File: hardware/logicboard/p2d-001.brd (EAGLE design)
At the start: 91 x 90 mm, 55 parts, among them IC1 74LS06N, IC2 4066N, J1 MKR, J2 GPIO, J3 Vcc, J4 RLY, J5 SPI, J7 DIN5, J8 DIN5, J9 DIN5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

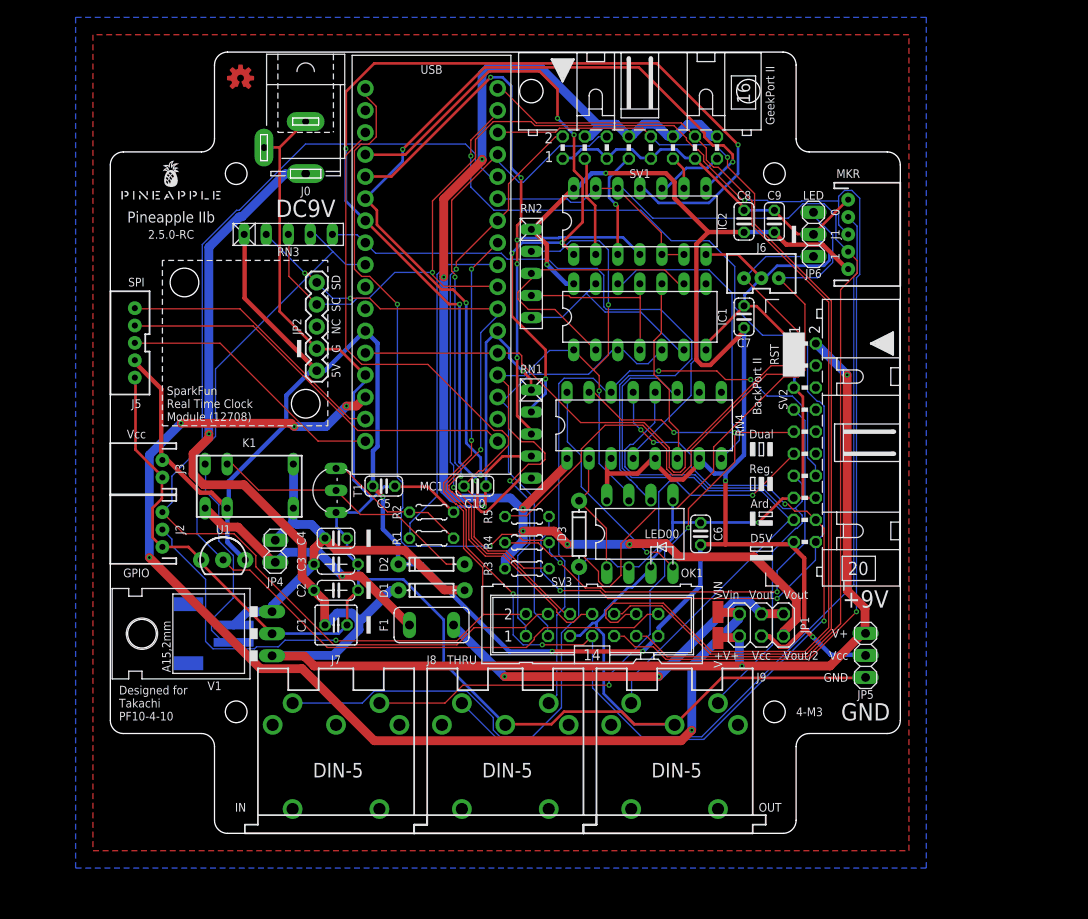
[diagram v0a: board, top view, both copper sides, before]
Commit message: Changed dimension of the board.
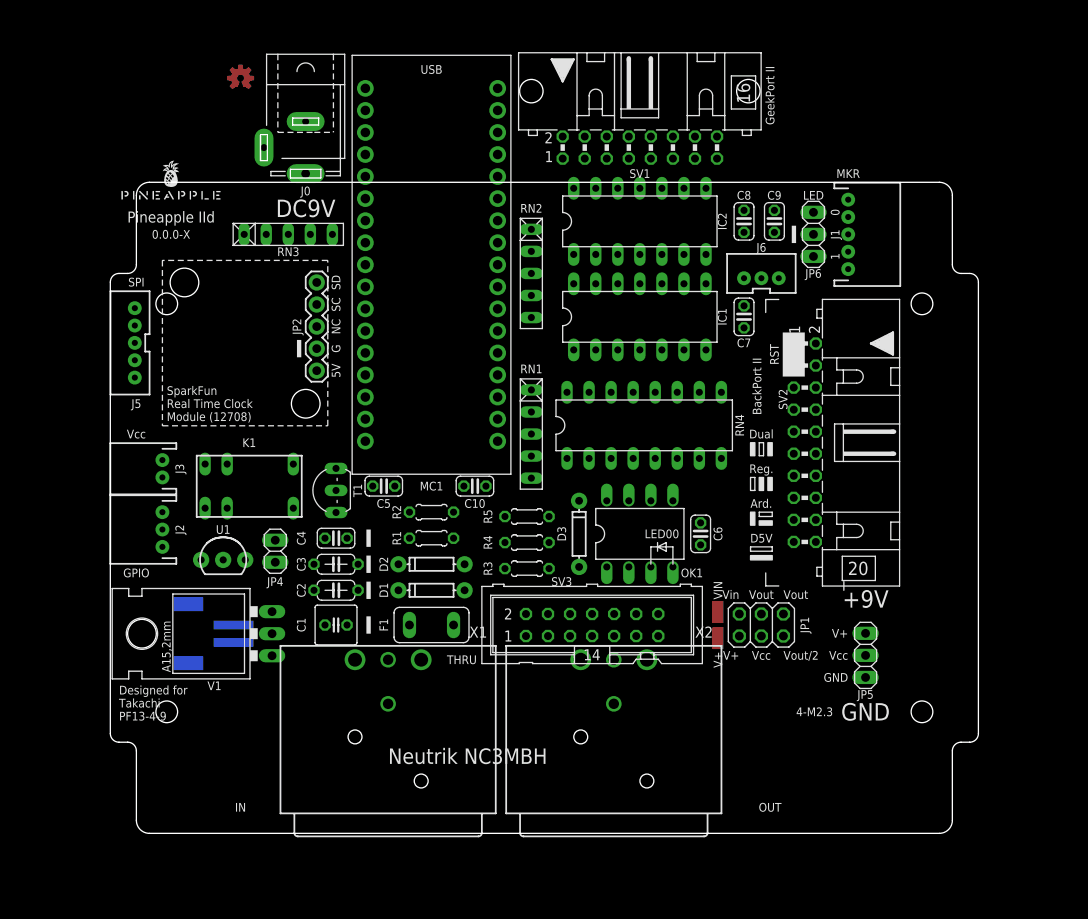
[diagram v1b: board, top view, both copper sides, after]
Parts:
- removed J7, J8, J9: DIN5, SparkFun-Connectors:DIN5-RA-PTH
- added X1, X2: NC3MBH, con-neutrik_ag:NC3MBH
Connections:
- net GND: no longer J8.2, J9.2
- net MIRTN: no longer J7.5
- net MISND: no longer J7.4
- net MORTN: no longer J9.5
- net MOSND: no longer J9.4
- net MTRTN: no longer J8.5
- net MTSND: no longer J8.4
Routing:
- net GND: track 393.3 -> 0.00 mm, vias 3 -> 0
- net VCC: track 314.4 -> 0.00 mm, vias 7 -> 0
- net V+: track 203.3 -> 0.00 mm, vias 3 -> 0
- net SCL: track 184.1 -> 0.00 mm, vias 3 -> 0
- net SDA: track 172.1 -> 0.00 mm, vias 5 -> 0
- net VCC/2: track 150.3 -> 0.00 mm, vias 6 -> 0
- net ANLG3: track 130.1 -> 0.00 mm, vias 4 -> 0
- net VIN: track 129.7 -> 0.00 mm, vias 5 -> 0
- net D7GATE: track 129.7 -> 0.00 mm
- net LED0: track 127.5 -> 0.00 mm, vias 4 -> 0
- net LED1: track 126.8 -> 0.00 mm, vias 3 -> 0
- net GPIO1: track 126.6 -> 0.00 mm
- net DTCT3: track 122.7 -> 0.00 mm
- net DTCT2: track 116.3 -> 0.00 mm, vias 1 -> 0
- net THS: track 107.1 -> 0.00 mm
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- removed copper zone on layer 1, net GND
- removed copper zone on layer 16, net GND
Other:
- board size 91 x 90 mm -> 100 x 75 mm
- board text added: "0.0.0-X"
- board text added: "4-M2.3"
- board text added: "Designed for Takachi PF13-4-9"
- board text added: "Neutrik NC3MBH"
- board text added: "Pineapple IId"
- board text removed: "2.5.0-RC"
- board text removed: "4-M3"
- board text removed: "Designed for Takachi PF10-4-10"
- board text removed: "Pineapple IIb"

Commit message: Put all parts on board.
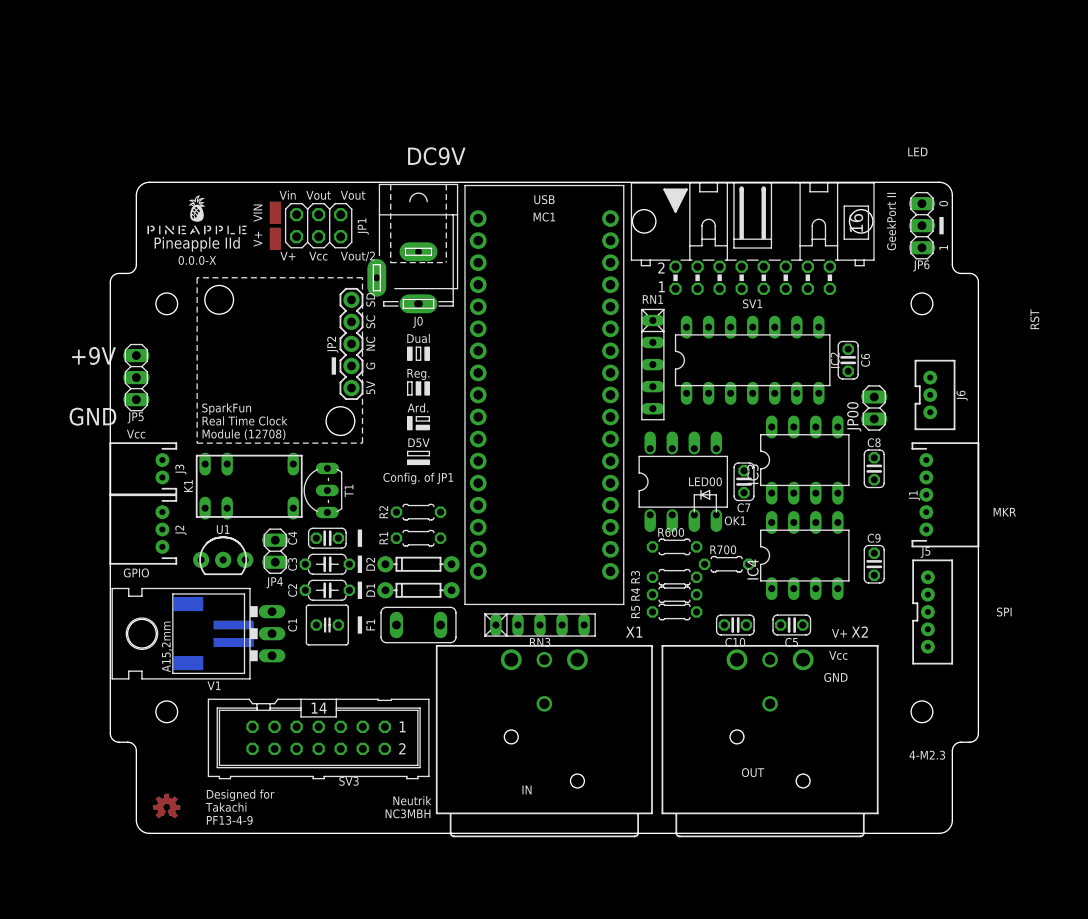
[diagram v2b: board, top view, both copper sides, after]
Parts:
- removed D3: (no value), SparkFun-DiscreteSemi:DIODE-1N4148
- removed IC1: 74LS06N, 74xx-us:DIL14
- removed RN2: 4.7k, resistor-net:RN-5
- removed RN4: 220, resistor-dil:DIL16
- removed SV2: (no value), con-ml:ML20L
- added IC3, IC4: MAX3468CPA, maxim:DIL08
- added JP00: (no value), pinhead:1X02
- added R600: 220, resistor:0204/5
- added R700: 120, resistor:0204/5
- moved J5 96.1 mm to (94.0, 25.5), turned to 270 degrees
- moved JP5 89.9 mm to (3.00, 52.5)
- moved LOGO1 84.4 mm to (6.50, 3.00)
- moved JP1 68.7 mm to (24.0, 70.0)
- moved V+ 68.7 mm to (19.0, 68.5)
- moved VIN 68.7 mm to (19.0, 71.5)
- moved RN3 53.5 mm to (49.5, 24.0)
- moved C5 49.6 mm to (78.5, 24.0)
- moved C9 41.1 mm to (88.0, 31.0)
- moved SV3 34.1 mm to (24.0, 11.0), turned to 180 degrees
- moved C10 34.0 mm to (72.0, 24.0)
- moved C8 32.2 mm to (88.0, 42.0)
- moved J1 31.3 mm to (94.0, 39.0)
- moved C6 26.2 mm to (85.0, 54.5)
- moved J6 24.4 mm to (95.0, 50.5), turned to 270 degrees
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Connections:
- removed net MIDIINSND: D3.C, OK1.1, RN4.2
- removed net MIRTN: D3.A, OK1.2, SV2.11
- removed net MISND: RN4.15, SV2.9
- removed net MO2RTN: RN4.9
- removed net MO2RTNRAW: IC1.12, RN4.8
- removed net MO2SND: RN4.10
- removed net MORTN: RN4.11, SV2.17
- removed net MORTNRAW: IC1.10, RN4.6
- removed net MOSND: RN4.12, SV2.13
- removed net MRX+: SV2.6
- removed net MRX-: SV2.8
- removed net MRXDTCT: SV2.4
- removed net MTRTN: RN4.13, SV2.18
- removed net MTRTNRAW: IC1.8, RN4.4
- removed net MTSND: RN4.14, SV2.14
- removed net MTX+: SV2.10
- removed net MTX-: SV2.12
- removed net NMO2RTN: IC1.13, IC1.6, RN2.5
- removed net NMORTN: IC1.11, IC1.4, RN2.4
- removed net NMTRTN: IC1.2, IC1.9, RN2.3
- net GND: now also IC3.5, IC4.5; no longer IC1.7, SV2.1, SV2.15, SV2.16, SV2.5
- net LED0: no longer SV2.7
- net LED1: no longer SV2.20
- net MNTRA: now also R600.1; no longer RN4.16
- net RST: no longer SV2.3
- net RX: no longer IC1.1, OK1.7, RN2.2
- net TX: no longer IC1.3, IC1.5
- net V+: no longer SV2.2
- net VCC: now also IC3.8, IC4.8; no longer IC1.14, RN2.1, RN4.3, RN4.5, RN4.7, SV2.19
- net VCC/2: now also R600.2; no longer RN4.1
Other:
- board text added: "Config. of JP1"
- board text removed: "BackPort II"
- board text removed: "THRU"

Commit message: Design of transceiver.
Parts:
- removed IC4: MAX3468CPA, maxim:DIL08
- removed JP00: (no value), pinhead:1X02
- added JP00RST, JP03SELFTERMINATE: (no value), pinhead:1X02
- moved C9 33.6 mm to (59.0, 14.0)
- moved C5 25.3 mm to (54.5, 16.0)
- moved C10 22.0 mm to (55.0, 10.0)
- moved RN3 20.6 mm to (29.5, 19.0)
- moved R3 19.8 mm to (46.0, 24.0)
- moved R700 11.4 mm to (82.0, 34.0)
- moved R4 10.6 mm to (55.0, 24.0)
- moved IC3 2.83 mm to (82.0, 41.0)
- moved J6 2.06 mm to (94.5, 48.5)
- moved R5 1.80 mm to (64.0, 24.0)
- moved J1 1.50 mm to (94.0, 37.5)
- moved C8 1.41 mm to (89.0, 41.0)
- moved R600 1.41 mm to (66.0, 34.0)
- moved JP5 1.12 mm to (4.00, 52.0)
- moved RN1 1.12 mm to (62.0, 55.0)
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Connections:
- new net DATA+: IC3.6, R700.1, X1.3, X2.3
- new net DATA-: IC3.7, JP03SELFTERMINATE.2, X1.2, X2.2
- new net N$1: JP03SELFTERMINATE.1, R700.2
- net GND: now also JP00RST.2, OK1.1, OK1.2, X1.1, X1.G, X2.1, X2.G; no longer IC4.5
- net LED1: now also IC3.2, IC3.3
- net RST: now also JP00RST.1
- net RX: now also IC3.1
- net TX: now also IC3.4
- net VCC: no longer IC4.8

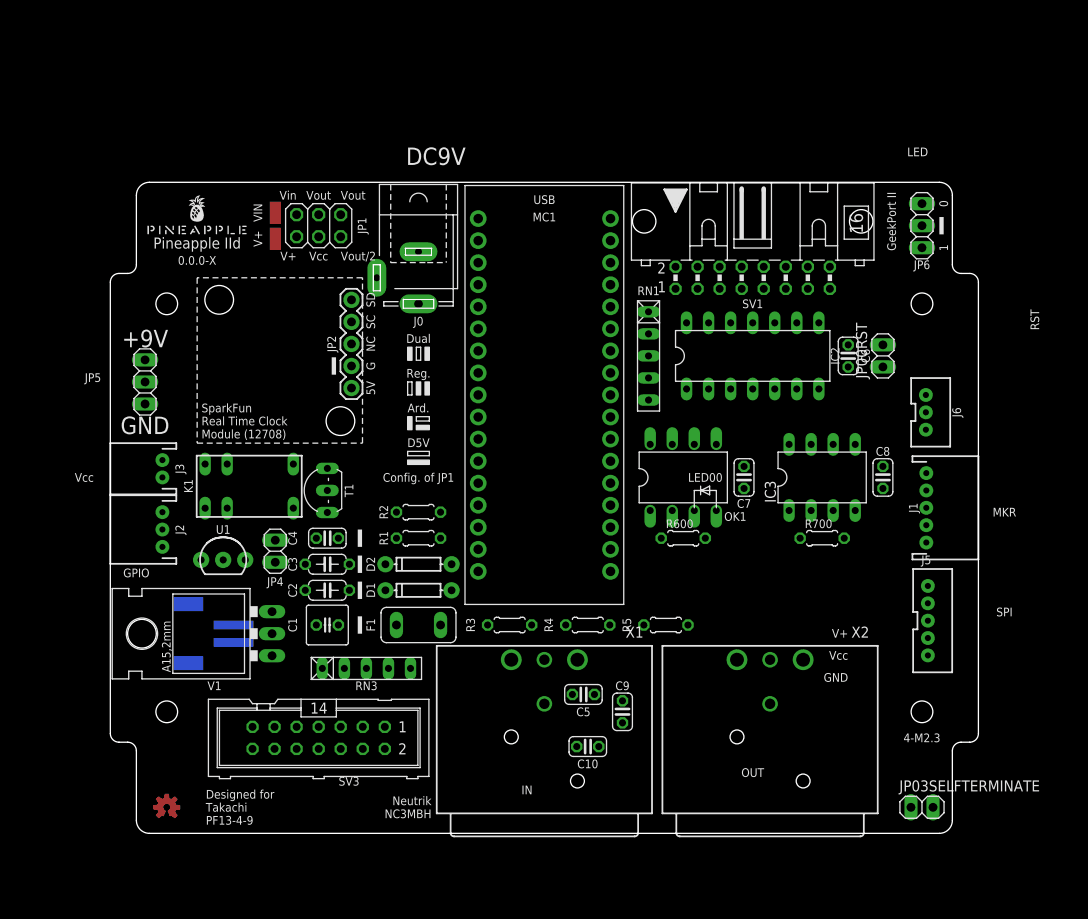
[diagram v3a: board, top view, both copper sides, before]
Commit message: Get MIDI back.
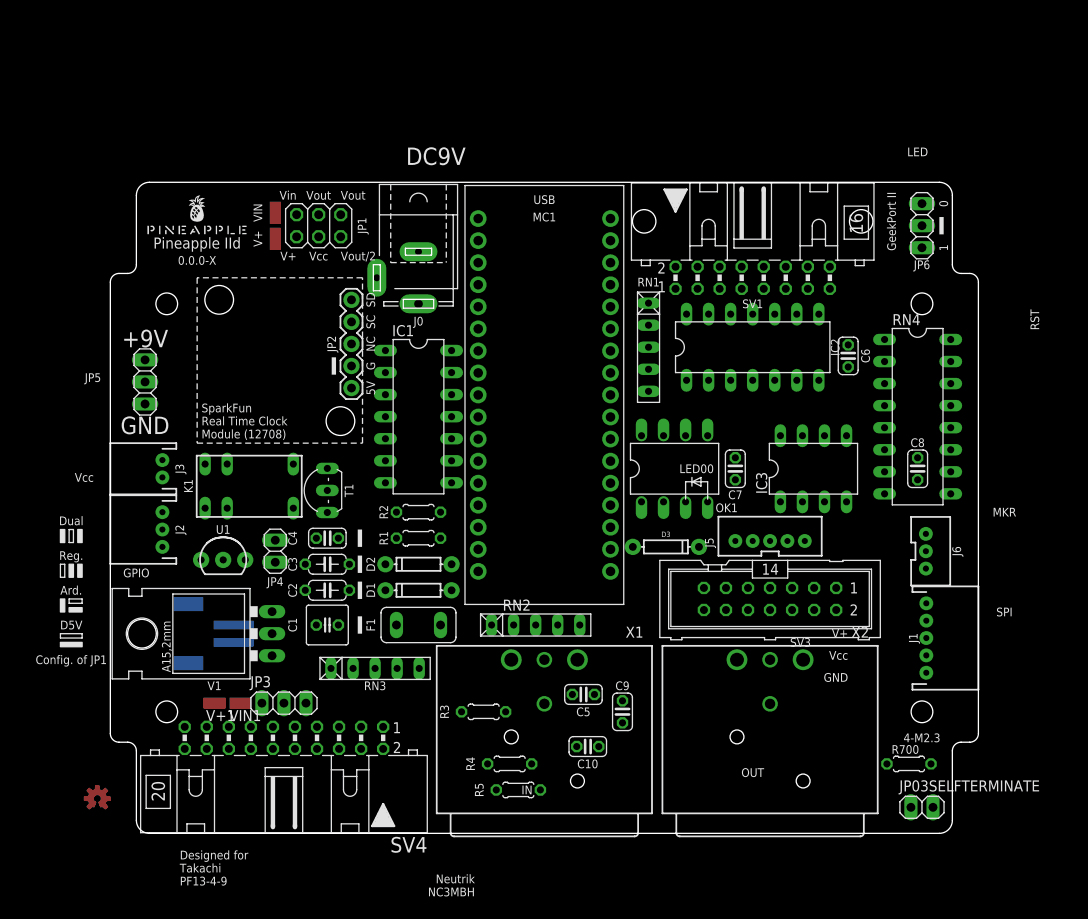
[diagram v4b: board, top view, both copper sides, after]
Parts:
- removed JP00RST: (no value), pinhead:1X02
- removed R600: 220, resistor:0204/5
- added D3: (no value), SparkFun-DiscreteSemi:DIODE-1N4148
- added IC1: 74LS06N, 74xx-us:DIL14
- added JP3: (no value), pinhead:1X03
- added RN2: 4.7k, resistor-net:RN-5
- added RN4: (no value), resistor-dil:DIL16
- added SV4: (no value), con-ml:ML20L
- added V+1, VIN1: (no value), wirepad:SMD1,27-2,54
- moved SV3 54.4 mm to (76.0, 27.0)
- moved R700 27.9 mm to (92.0, 8.00)
- moved R5 25.5 mm to (47.0, 5.00)
- moved J5 20.1 mm to (76.0, 33.5), turned to 0 degrees
- moved R4 18.4 mm to (46.0, 8.00)
- moved J6 16.0 mm to (94.5, 32.5)
- moved J1 15.0 mm to (94.0, 22.5)
- moved R3 10.4 mm to (43.0, 14.0)
- moved LOGO1 8.06 mm to (-1.50, 4.00)
- moved C8 4.12 mm to (93.0, 42.0)
- moved C7 1.41 mm to (72.0, 42.0)
- moved IC3 1.41 mm to (81.0, 42.0)
- moved OK1 1.41 mm to (65.0, 42.0)
- moved IC2 1.00 mm to (74.0, 56.0)
- moved RN1 1.00 mm to (62.0, 56.0)
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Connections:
- new net DMXRX: IC3.1, JP3.1, VIN1.1
- new net MI: IC1.1, JP3.3, OK1.7
- new net MIN: RN2.2
- new net MIRTN: D3.A, OK1.2
- new net MISND: RN4.15
- new net MO2RTN: RN4.9
- new net MO2SND: RN4.10
- new net MORTN: RN4.11
- new net MOSND: RN4.12
- new net MTRTN: RN4.13
- new net MTSND: RN4.14
- new net N$2: D3.C, OK1.1, RN4.2
- new net N$3: IC1.10, RN4.6
- new net N$4: IC1.12, RN4.8
- new net N$5: IC1.8, RN4.4
- new net NMO2RTN: IC1.13, IC1.6, RN2.5
- new net NMORTN: IC1.11, IC1.4, RN2.4
- new net NMTRTN: IC1.2, IC1.9, RN2.3
- net GND: now also IC1.7; no longer JP00RST.2, OK1.1, OK1.2
- net MNTRA: now also RN4.1; no longer R600.1
- net RST: no longer JP00RST.1
- net RX: now also JP3.2, V+1.1; no longer IC3.1
- net TX: now also IC1.3, IC1.5
- net VCC: now also IC1.14, RN2.1, RN4.3, RN4.5, RN4.7
- net VCC/2: now also RN4.16; no longer R600.2

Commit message: Try. Error.
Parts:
- removed SV4: (no value), con-ml:ML20L
- added JP7: (no value), pinhead:2X10
- moved V+1 63.5 mm to (47.0, 68.0)
- moved VIN1 62.4 mm to (51.0, 66.0)
- moved JP3 54.4 mm to (50.5, 60.0)
- moved RN3 46.6 mm to (76.0, 9.00)
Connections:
- net GND: now also JP7.1, JP7.15, JP7.5
- net LED0: now also JP7.7
- net MIRTN: now also JP7.11
- net MISND: now also JP7.9
- net MORTN: now also JP7.17
- net MOSND: now also JP7.13
- net RST: now also JP7.3
- net VCC: now also JP7.19
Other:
- board text added: "IN4"
- board text added: "IN5"
- board text added: "Install Neutrik NC3MBH"
- board text added: "LED0"
- board text added: "OUT4"
- board text added: "OUT5"
- board text removed: "Neutrik NC3MBH"

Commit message: Routing test.
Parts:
- removed V+1, VIN1: (no value), wirepad:SMD1,27-2,54
- added A, B, DMXRX, RX, V/2, VO: (no value), wirepad:SMD1,27-2,54
- SV3: device con-ml:ML14 -> pinhead:2X07
- moved J5 61.9 mm to (20.5, 6.00), turned to 180 degrees
- moved R5 57.6 mm to (83.5, 49.5)
- moved R4 50.9 mm to (75.5, 49.5)
- moved C5 46.6 mm to (35.5, 58.5)
- moved R3 43.1 mm to (67.5, 49.5)
- moved C10 39.8 mm to (91.0, 27.0), turned to 90 degrees
- moved JP3 39.4 mm to (81.0, 35.0)
- moved RN3 30.3 mm to (50.0, 24.5)
- moved LOGO1 22.1 mm to (20.5, 2.50)
- moved RN2 19.5 mm to (30.0, 19.5)
- moved C9 13.2 mm to (61.0, 27.0)
- moved C8 6.50 mm to (86.5, 42.0)
- moved D3 2.24 mm to (65.0, 35.0)
- moved JP03SELFTERMINATE 1.50 mm to (92.0, 3.00)
- moved JP1 1.50 mm to (22.5, 70.0)
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- renumbered JP7 to SV2
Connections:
- net DMXRX: now also DMXRX.1; no longer VIN1.1
- net RX: now also RX.1; no longer V+1.1
- net VCC/2: now also V/2.1
- net VOUT: now also VO.1
- net VOUTRAW: now also B.1
- net VOUTRAW2: now also A.1
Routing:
- net GND: track 0.00 -> 415.1 mm
- net VCC: track 0.00 -> 391.7 mm, vias 0 -> 6
- net VCC/2: track 0.00 -> 293.4 mm, vias 0 -> 4
- net LED0: track 0.00 -> 157.0 mm, vias 0 -> 2
- net AREF: track 0.00 -> 144.1 mm
- net MOSND: track 0.00 -> 137.9 mm
- net GPIO1: track 0.00 -> 129.7 mm, vias 0 -> 4
- net THS: track 0.00 -> 129.6 mm, vias 0 -> 3
- net MORTN: track 0.00 -> 126.1 mm
- net SCL: track 0.00 -> 122.7 mm, vias 0 -> 4
- net MISND: track 0.00 -> 122.4 mm, vias 0 -> 2
- net GPIO0: track 0.00 -> 121.8 mm, vias 0 -> 4
- net SDA: track 0.00 -> 120.2 mm, vias 0 -> 2
- net V+: track 0.00 -> 118.2 mm, vias 0 -> 1
- net N$4: track 0.00 -> 108.3 mm, vias 0 -> 1
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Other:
- board text added: "00"
- board text added: "01"
- board text added: "02"
- board text added: "03"
- board text added: "2"
- board text added: "D7"
- board text added: "DMXRX"
- board text added: "G0"
- board text added: "G1"
- board text added: "MIDIIN"
- board text added: "RX"
- board text added: "TH"
- board text added: "TX"
- board text added: "V"
- board text added: "Vcc/2"
- board text removed: "Vout/2"

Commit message: First try.
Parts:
- JP03SELFTERMINATE: device pinhead:1X02 -> pinhead:1X02/90
- moved LOGO1 71.0 mm to (6.00, 72.0)
- moved U$1 14.5 mm to (19.5, 58.0)
- moved JP1 3.35 mm to (19.5, 68.5)
- moved V+ 3.35 mm to (14.5, 67.0)
- moved V/2 3.35 mm to (24.5, 67.0)
- moved VIN 3.35 mm to (14.5, 70.0)
- moved VO 3.35 mm to (24.5, 70.0)
- moved JP03SELFTERMINATE 3.00 mm to (92.0, 0.00), turned to 180 degrees
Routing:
- net VCC/2: track 293.4 -> 128.4 mm, vias 4 -> 2
- net VIN: track 57.2 -> 118.6 mm, vias 8 -> 4
- net LED0: track 157.0 -> 122.5 mm, vias 2 -> 4
- net AREF: track 144.1 -> 119.6 mm
- net MOSND: track 137.9 -> 114.8 mm, vias 0 -> 1
- net DATA+: track 93.5 -> 74.9 mm
- net V+: track 118.2 -> 100.9 mm
- net SCL: track 122.7 -> 105.6 mm, vias 4 -> 1
- net ANLG2: track 75.1 -> 88.4 mm, vias 3 -> 2
- net GPIO0: track 121.8 -> 134.6 mm, vias 4 -> 3
- net N$4: track 108.3 -> 95.7 mm, vias 1 -> 4
- net MIRTN: track 66.9 -> 79.1 mm, vias 3 -> 0
- net THS: track 129.6 -> 118.4 mm
- net DTCT2: track 78.9 -> 67.9 mm, vias 4 -> 2
- net N$5: track 85.0 -> 74.6 mm, vias 2 -> 0
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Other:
- board text added: "Arduino Reg."
- board text added: "BackPort II"
- board text added: "Close Here"
- board text added: "Direct 5V"
- board text added: "Dual Reg."
- board text added: "Pineapple IId 0.0.0-X"
- board text added: "Single Reg."
- board text added: "TestPort II"
- board text removed: "0.0.0-X"
- board text removed: "Ard."
- board text removed: "D5V"
- board text removed: "Dual"
- board text removed: "Pineapple IId"
- board text removed: "Reg."

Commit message: Looks ok.
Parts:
- moved C7 40.1 mm to (35.5, 58.5), turned to 0 degrees
- moved C9 38.9 mm to (87.0, 56.0)
- moved C10 30.0 mm to (61.0, 27.0), turned to 270 degrees
- moved C5 19.6 mm to (29.0, 40.0), turned to 270 degrees
- moved C6 19.4 mm to (71.5, 42.0)
- moved C8 14.1 mm to (84.5, 56.0)
- moved RN4 1.00 mm to (93.5, 47.5)
- moved J1 0.50 mm to (94.0, 23.0)
- renumbered JP03SELFTERMINATE to JP10, R700 to R10
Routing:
- net TX: track 89.2 -> 164.7 mm
- net AREF: track 119.6 -> 64.5 mm, vias 0 -> 4
- net VCC/2: track 128.4 -> 180.8 mm, vias 2 -> 6
- net GND: track 418.5 -> 457.2 mm, vias 3 -> 5
- net VOUT: track 102.1 -> 64.0 mm
- net SCL: track 105.6 -> 135.0 mm, vias 1 -> 2
- net ANLG0: track 51.2 -> 79.5 mm, vias 2 -> 9
- net MI: track 74.3 -> 91.5 mm, vias 4 -> 3
- net ANLG1: track 72.4 -> 56.1 mm, vias 2 -> 3
- net MISND: track 130.3 -> 114.5 mm, vias 1 -> 3
- net N$5: track 74.6 -> 90.4 mm, vias 0 -> 2
- net VIN: track 118.6 -> 132.5 mm, vias 4 -> 2
- net LED0: track 122.5 -> 135.8 mm, vias 4 -> 2
- net VCC: track 381.5 -> 393.9 mm, vias 4 -> 8
- net N$3: track 62.8 -> 75.0 mm
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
